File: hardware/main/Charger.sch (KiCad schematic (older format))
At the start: 24 parts

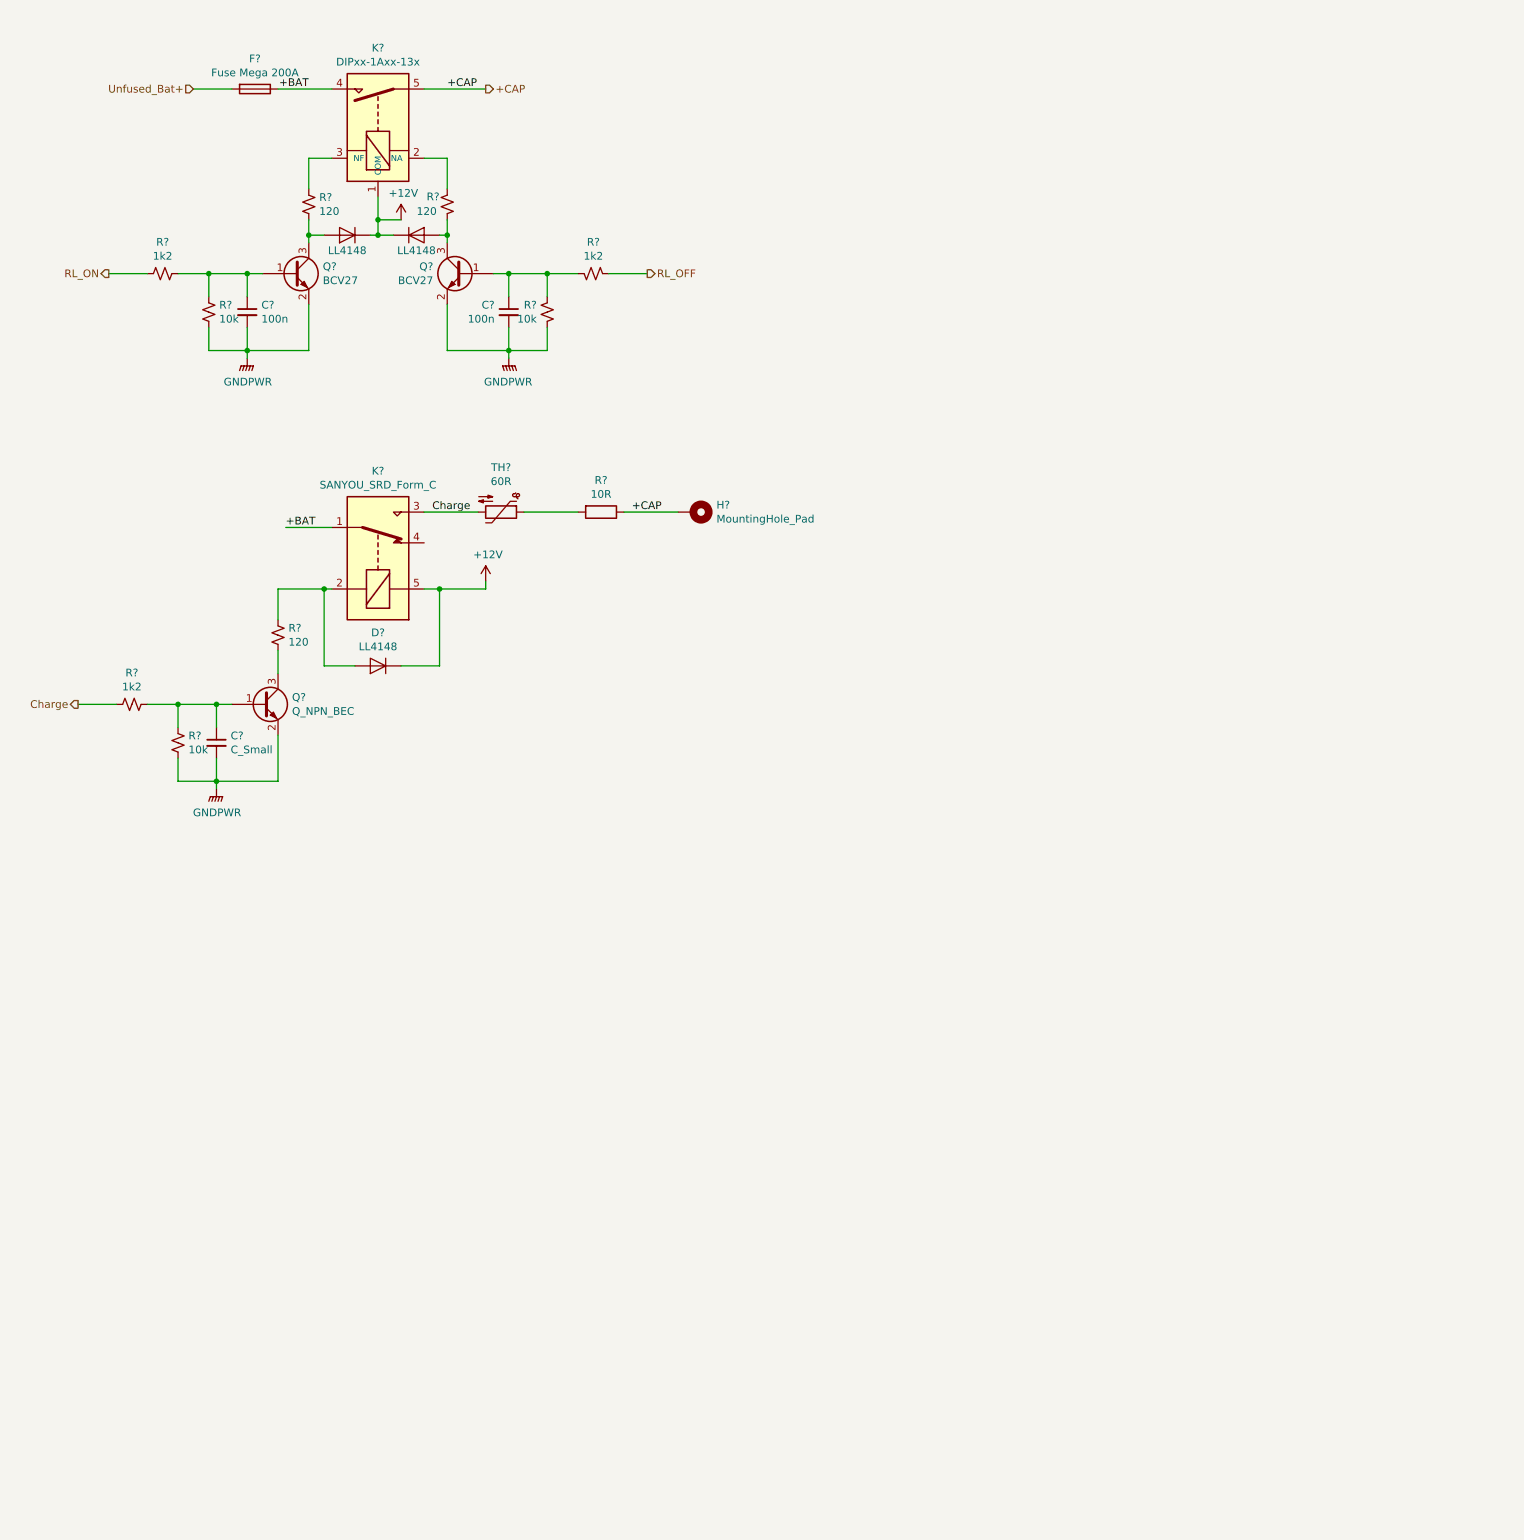
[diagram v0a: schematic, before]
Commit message: Primeira versão do esquematico finalizada Falta DRC
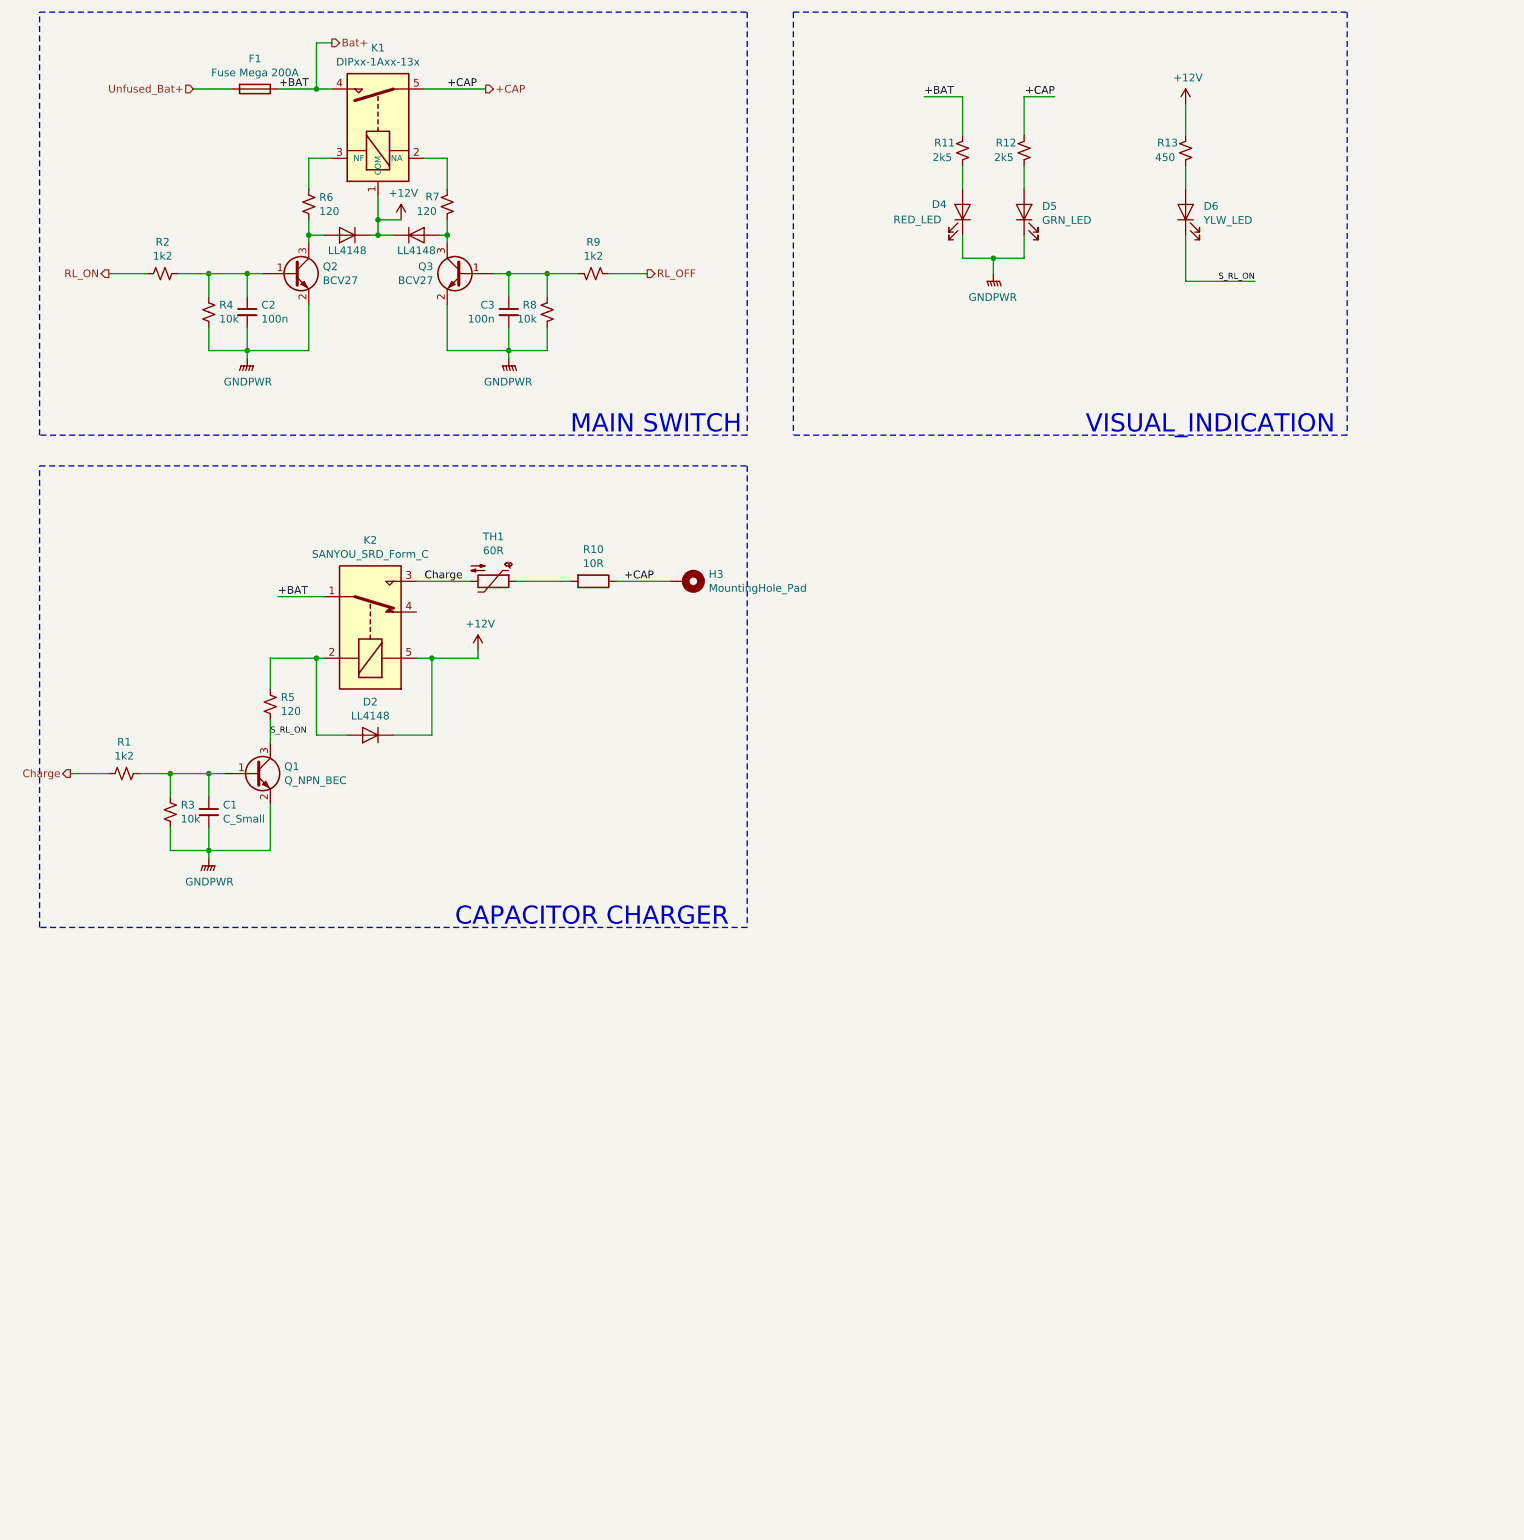
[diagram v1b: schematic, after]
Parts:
- added D4: RED_LED, symbol Device:LED
- added D5: GRN_LED, symbol Device:LED
- added D6: YLW_LED, symbol Device:LED
- added R11, R12: 2k5, symbol Device:R_Small_US
- added R13: 450, symbol Device:R_Small_US
- gave numbers to parts that had none: 24
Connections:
- net +12V: now also R13.1
- net +CAP: now also R12.1
- net GNDPWR: now also D4.1 (K), D5.1 (K)
- net S_RL_ON: now reaches Q1.3 (C), R5.2
- net S_RL_ON: now also D6.1 (K)
- net +BAT renamed Bat+
- net Bat+: now also R11.1
- new net: D4.2 (A), R11.2
- new net: D5.2 (A), R12.2
- new net: D6.2 (A), R13.2
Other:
- note added: "CAPACITOR CHARGER"
- note added: "MAIN SWITCH"
- note added: "VISUAL_INDICATION\n"
- moved on the sheet: C1, D2, H3, K2, Q1, R1, R10, R3, R5, TH1

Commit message: O fusivel do sistema foi movido pro GND
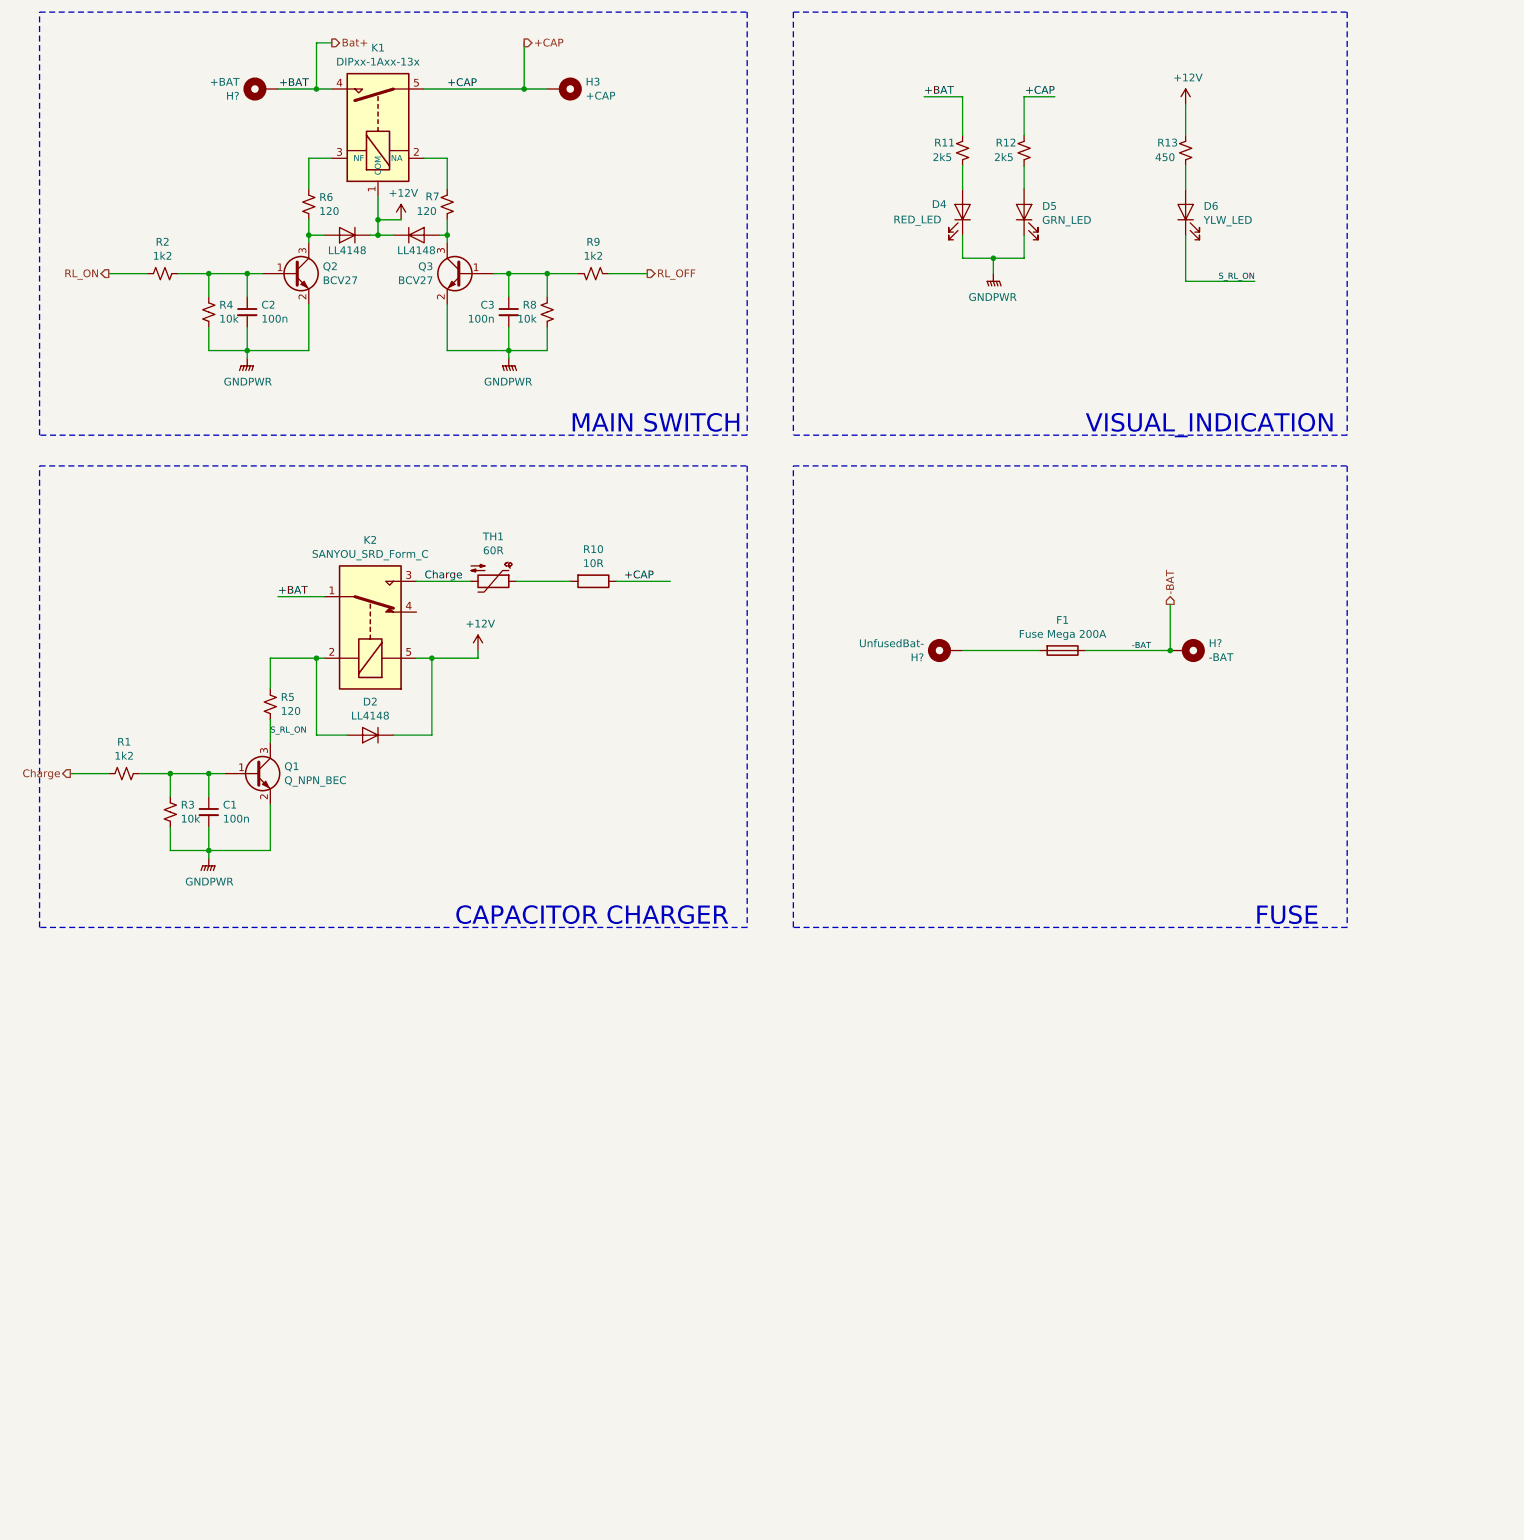
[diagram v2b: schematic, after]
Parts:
- added H?: UnfusedBat-, symbol Mechanical:MountingHole_Pad
- added H?: -BAT, symbol Mechanical:MountingHole_Pad
- added H?: +BAT, symbol Mechanical:MountingHole_Pad
- C1: value C_Small -> 100n
- H3: value MountingHole_Pad -> +CAP
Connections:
- net Bat+: now also H?.1; no longer F1.1
- net Unfused_Bat+: no longer names the net of F1.2
- net Unfused_Bat+: now also H?.1
- new net -BAT: F1.1, H?.1
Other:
- note added: "FUSE"
- moved on the sheet: F1, H3
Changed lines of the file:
@@
 L Device:Fuse F1
 U 1 1 5C9E0E43
-P 2050 1250
-F 0 "F1" V 1853 1250 50  0000 C CNN
-F 1 "Fuse Mega 200A" V 1944 1250 50  0000 C CNN
-F 2 "" V 1980 1250 50  0001 C CNN
-F 3 "~" H 2050 1250 50  0001 C CNN
-	1    2050 1250
+P 7300 4900
+F 0 "F1" V 7103 4900 50  0000 C CNN
+F 1 "Fuse Mega 200A" V 7194 4900 50  0000 C CNN
+F 2 "" V 7230 4900 50  0001 C CNN
+F 3 "~" H 7300 4900 50  0001 C CNN
+	1    7300 4900
 	0    1    1    0
 $EndComp
@@
 $EndComp
 Wire Wire Line
-	1650 1250 1900 1250
-Wire Wire Line
 	3750 4450 4100 4450
 Text Label 3400 4450 2    50   ~ 0
@@
 P 1750 5950
 F 0 "C1" H 1842 5996 50  0000 L CNN
-F 1 "C_Small" H 1842 5905 50  0000 L CNN
+F 1 "100n" H 1842 5905 50  0000 L CNN
 F 2 "" H 1750 5950 50  0001 C CNN
 F 3 "~" H 1750 5950 50  0001 C CNN
@@
 Text Label 3300 1250 0    50   ~ 0
 +CAP
-Wire Wire Line
-	2200 1250 2450 1250
 $Comp
 L Mechanical:MountingHole_Pad H3
 U 1 1 5C9E3AC0
-P 4850 4450
-F 0 "H3" V 4804 4600 50  0000 L CNN
-F 1 "MountingHole_Pad" V 4895 4600 50  0000 L CNN
-F 2 "" H 4850 4450 50  0001 C CNN
-F 3 "~" H 4850 4450 50  0001 C CNN
-	1    4850 4450
+P 4050 1250
+F 0 "H3" V 4004 1400 50  0000 L CNN
+F 1 "+CAP" V 4095 1400 50  0000 L CNN
+F 2 "" H 4050 1250 50  0001 C CNN
+F 3 "~" H 4050 1250 50  0001 C CNN
+	1    4050 1250
 	0    1    1    0
 $EndComp
-Text HLabel 1650 1250 0    50   Input ~ 0
-Unfused_Bat+
-Text HLabel 3550 1250 2    50   Output ~ 0
+Text HLabel 3800 950  2    50   Output ~ 0
 +CAP
-Wire Wire Line
-	3150 1250 3550 1250
 Wire Wire Line
 	2150 4950 2450 4950
@@
 Wire Wire Line
 	2450 950  2450 1250
-Connection ~ 2450 1250
 Wire Wire Line
 	2450 1250 2550 1250
@@
 Text Notes 7450 3500 0    118  ~ 0
 VISUAL_INDICATION\n
+$Comp
+L Mechanical:MountingHole_Pad H?
+U 1 1 5CA37EF3
+P 6550 4900
+F 0 "H?" V 6504 5050 50  0000 L CNN
+F 1 "UnfusedBat-" V 6595 5050 50  0000 L CNN
+F 2 "" H 6550 4900 50  0001 C CNN
+F 3 "~" H 6550 4900 50  0001 C CNN
+	1    6550 4900
+	0    -1   -1   0
+$EndComp
+Wire Wire Line
+	6650 4900 7150 4900
+$Comp
+L Mechanical:MountingHole_Pad H?
+U 1 1 5CA39D8E
+P 8100 4900
+F 0 "H?" V 8054 5050 50  0000 L CNN
+F 1 "-BAT" V 8145 5050 50  0000 L CNN
+F 2 "" H 8100 4900 50  0001 C CNN
+F 3 "~" H 8100 4900 50  0001 C CNN
+	1    8100 4900
+	0    1    1    0
+$EndComp
+Wire Wire Line
+	7450 4900 8000 4900
+Text Label 7750 4900 0    39   ~ 0
+-BAT
+Wire Notes Line
+	5550 3700 9150 3700
+Wire Notes Line
+	9150 3700 9150 6700
+Wire Notes Line
+	9150 6700 5550 6700
+Wire Notes Line
+	5550 6700 5550 3700
+Text Notes 8550 6700 0    118  ~ 0
+FUSE
+Wire Wire Line
+	3150 1250 3800 1250
+Wire Wire Line
+	3800 950  3800 1250
+Connection ~ 3800 1250
+Wire Wire Line
+	3800 1250 3950 1250
+Wire Wire Line
+	2450 1250 2200 1250
+Connection ~ 2450 1250
+$Comp
+L Mechanical:MountingHole_Pad H?
+U 1 1 5CA4A13E
+P 2100 1250
+F 0 "H?" V 2054 1400 50  0000 L CNN
+F 1 "+BAT" V 2145 1400 50  0000 L CNN
+F 2 "" H 2100 1250 50  0001 C CNN
+F 3 "~" H 2100 1250 50  0001 C CNN
+	1    2100 1250
+	0    -1   -1   0
+$EndComp
+Text HLabel 8000 4600 1    50   Output ~ 0
+-BAT
+Wire Wire Line
+	8000 4600 8000 4900
+Connection ~ 8000 4900
 $EndSCHEMATC

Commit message: Abstração do esquemático modificada para separar as duas placas e mostrar a conexão entre elas na folha principal
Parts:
- added H? (x4): MountingHole, MountingHole:MountingHole_3.2mm_M3, symbol Mechanical:MountingHole
- H?: value UnfusedBat- -> U_BAT-
- H?: value -BAT -> F_BAT-
- H?: value +BAT -> U_BAT+
- K1: symbol High_current_rele:DIPxx-1Axx-13x -> main-rescue:DIPxx-1Axx-13x-High_current_rele
- K2: symbol Relay:SANYOU_SRD_Form_C -> main-rescue:SANYOU_SRD_Form_C-Relay
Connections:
- net -BAT is gone; now on net GNDPWR: F1.1, H?.1
- net U_BAT-: now reaches F1.2, H?.1
- net Bat+ renamed U_BAT+
- net U_BAT+: no longer K2.1
- new net +BAT: K2.1
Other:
- note added: "MAIN FUSE"
- note removed: "FUSE"
- moved on the sheet: C1, D2, H?, K2, Q1, R1, R10, R3, R5, TH1
